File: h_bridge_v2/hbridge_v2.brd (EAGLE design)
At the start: 92.3 x 48.2 mm, 28 parts, among them J2 1X2-3.5MM, J3 1X2-3.5MM, J4 AVR_SPI_PROG_3X2OFFSET_PADS, Q5 200mA/40V, Q6 200mA/40V, Q7 200mA/40V, Q8 200mA/40V, U1 328P, Y1 16MHz

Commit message: replaced the resonator with through hole one
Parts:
- removed Y1: 16MHz, SparkFun-Clocks:RESONATOR-SMD-3.2X1.3
- added Y2: (no value), SparkFun-Clocks:RESONATOR-PTH-7.6X3.8
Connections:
- net GND: now also Y2.2; no longer Y1.2
- net N$4: now also Y2.3; no longer Y1.3
- net N$5: now also Y2.1; no longer Y1.1
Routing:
- net GND: track 8.20 -> 2.41 mm
- net N$15: track 20.8 -> 25.1 mm
- net 5V: track 30.8 -> 33.2 mm
- net N$4: track 3.75 -> 4.88 mm

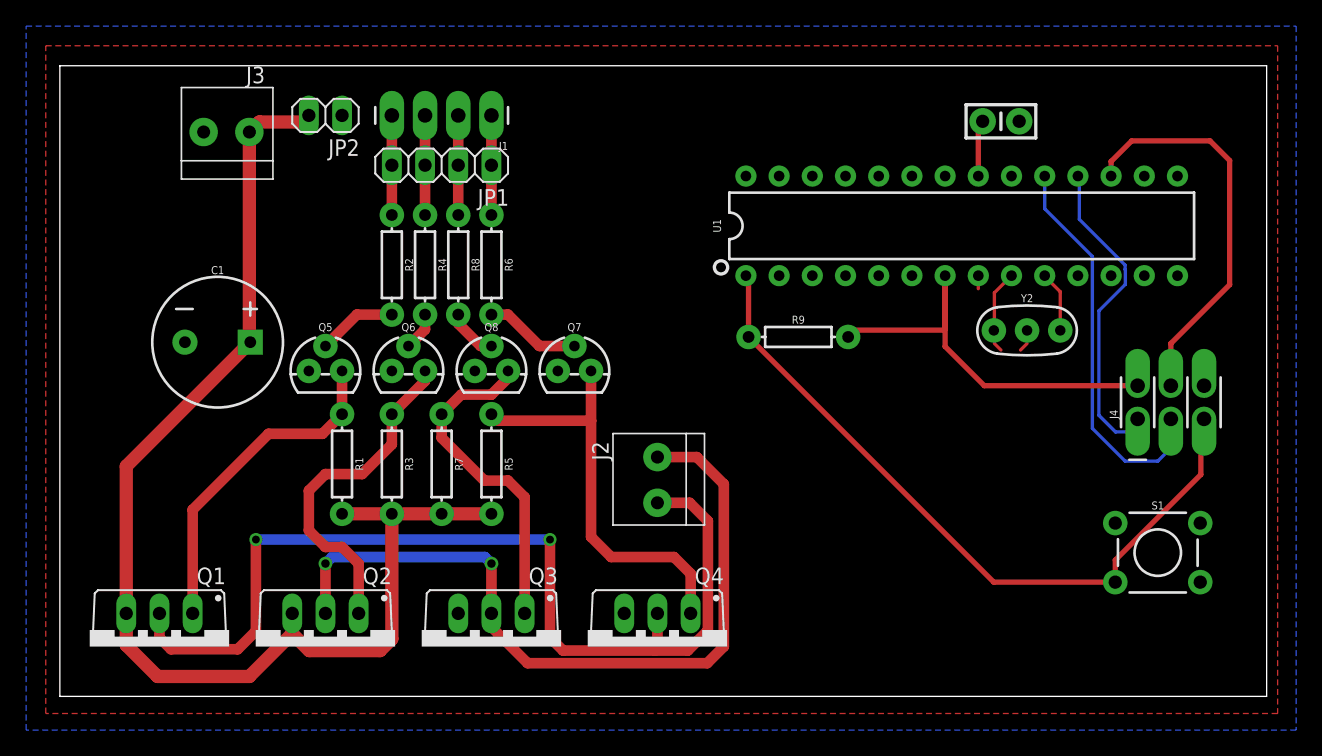
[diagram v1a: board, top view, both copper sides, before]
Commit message: added connections to PWM pins
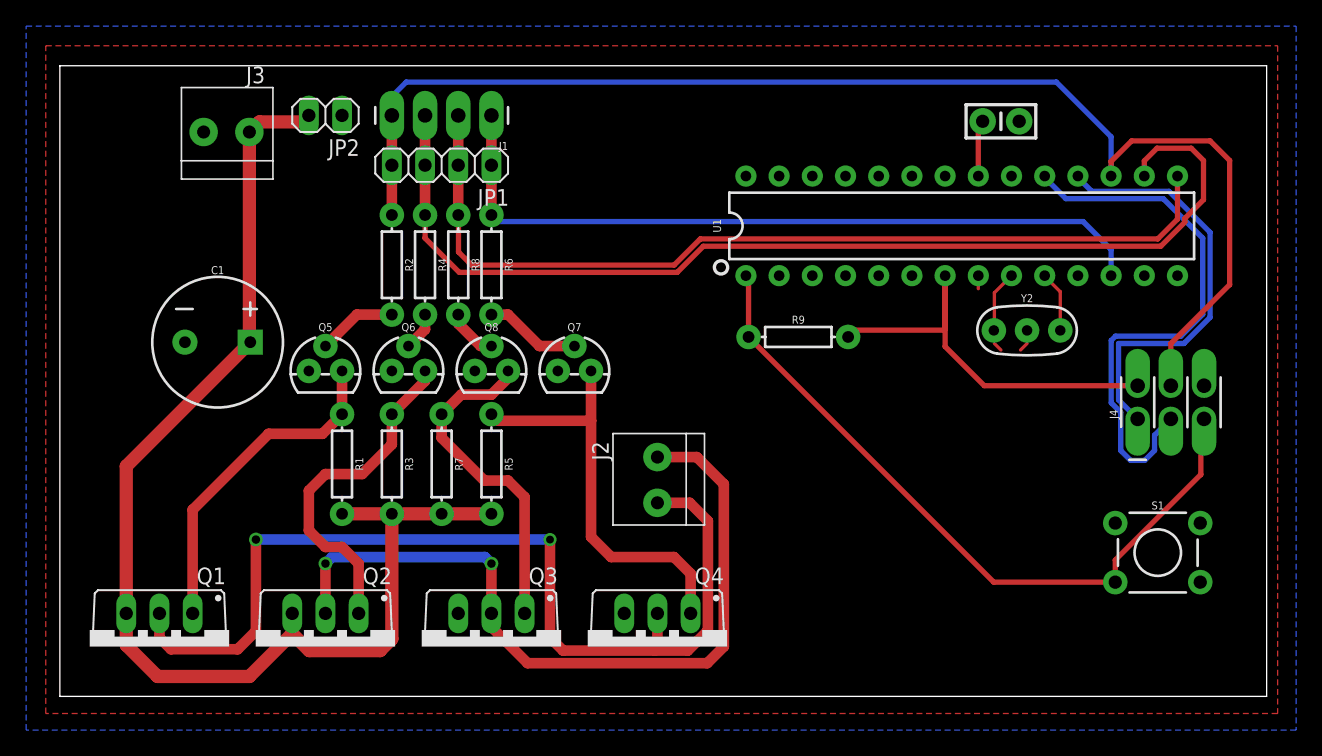
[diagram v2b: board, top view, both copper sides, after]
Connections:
- removed net N$18: J4.4, U1.17
- net Q1_INPUT: now also J4.4, U1.17
- net Q2_INPUT: now also U1.16
- net Q3_INPUT: now also U1.15
- net Q4_INPUT: now also U1.12
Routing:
- net Q1_INPUT: track 7.62 -> 99.8 mm
- net Q2_INPUT: track 7.62 -> 82.0 mm
- net Q3_INPUT: track 7.62 -> 70.6 mm
- net Q4_INPUT: track 7.62 -> 58.1 mm
- net N$18: track 30.6 -> 0.00 mm
- net N$16: track 30.5 -> 42.6 mm
- net N$15: track 25.1 -> 32.8 mm
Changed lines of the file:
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@@
 <drawing>
 <settings>
-<setting alwaysvectorfont="no"/>
+<setting alwaysvectorfont="yes"/>
 <setting verticaltext="up"/>
 </settings>
@@
 <wire x1="38.5" y1="3.5052" x2="37.5" y2="4.5052" width="0.8128" layer="1"/>
 <via x="37.5" y="12" extent="1-16" drill="0.6"/>
-<via x="15" y="12" extent="1-16" drill="0.6"/>
+<via x="15" y="12" extent="1-16" drill="0.65"/>
 <wire x1="15" y1="12" x2="15" y2="5" width="0.8128" layer="1"/>
 <wire x1="37.5" y1="4.5052" x2="37.5" y2="12" width="0.8128" layer="1"/>
@@
 <wire x1="27.94" y1="44.45" x2="27.94" y2="40.64" width="0.8128" layer="1"/>
 <wire x1="27.94" y1="36.83" x2="27.94" y2="40.64" width="0.8128" layer="1"/>
+<contactref element="U1" pad="16"/>
+<wire x1="82.97" y1="39.81" x2="82.97" y2="40.97" width="0.4064" layer="1"/>
+<wire x1="82.97" y1="40.97" x2="83.9412" y2="41.9412" width="0.4064" layer="1"/>
+<wire x1="86.5588" y1="41.9412" x2="87.5" y2="41" width="0.4064" layer="1"/>
+<wire x1="87.5" y1="41" x2="87.5" y2="38" width="0.4064" layer="1"/>
+<wire x1="86.0688" y1="36.5688" x2="86.0688" y2="36.27853125" width="0.4064" layer="1"/>
+<wire x1="86.0688" y1="36.27853125" x2="84.23146875" y2="34.4412" width="0.4064" layer="1"/>
+<wire x1="87.5" y1="38" x2="86.0688" y2="36.5688" width="0.4064" layer="1"/>
+<wire x1="49.23146875" y1="34.4412" x2="47.23146875" y2="32.4412" width="0.4064" layer="1"/>
+<wire x1="47.23146875" y1="32.4412" x2="30.5588" y2="32.4412" width="0.4064" layer="1"/>
+<wire x1="84.23146875" y1="34.4412" x2="49.23146875" y2="34.4412" width="0.4064" layer="1"/>
+<wire x1="27.94" y1="35.06" x2="27.94" y2="36.83" width="0.4064" layer="1"/>
+<wire x1="83.9412" y1="41.9412" x2="86.5588" y2="41.9412" width="0.4064" layer="1"/>
+<wire x1="30.5588" y1="32.4412" x2="27.94" y2="35.06" width="0.4064" layer="1"/>
 </signal>
 <signal name="N$6">
@@
 <wire x1="25.4" y1="44.45" x2="25.4" y2="40.64" width="0.8128" layer="1"/>
 <wire x1="25.4" y1="40.64" x2="25.4" y2="36.83" width="0.8128" layer="1"/>
+<contactref element="J4" pad="4"/>
+<contactref element="U1" pad="17"/>
+<wire x1="85" y1="23.77" x2="85" y2="27" width="0.4064" layer="1"/>
+<wire x1="89.5" y1="31.5" x2="89.5" y2="41" width="0.4064" layer="1"/>
+<wire x1="89.5" y1="41" x2="88" y2="42.5" width="0.4064" layer="1"/>
+<wire x1="88" y1="42.5" x2="82" y2="42.5" width="0.4064" layer="1"/>
+<wire x1="82" y1="42.5" x2="80.43" y2="40.93" width="0.4064" layer="1"/>
+<wire x1="80.43" y1="40.93" x2="80.43" y2="39.81" width="0.4064" layer="1"/>
+<wire x1="85" y1="27" x2="89.5" y2="31.5" width="0.4064" layer="1"/>
+<wire x1="25.4" y1="44.45" x2="25.4" y2="45.9" width="0.4064" layer="16"/>
+<wire x1="25.4" y1="45.9" x2="26.5" y2="47" width="0.4064" layer="16"/>
+<wire x1="26.5" y1="47" x2="76.24" y2="47" width="0.4064" layer="16"/>
+<wire x1="80.43" y1="42.81" x2="80.43" y2="39.81" width="0.4064" layer="16"/>
+<wire x1="80.43" y1="42.81" x2="76.24" y2="47" width="0.4064" layer="16"/>
 </signal>
 <signal name="Q4_INPUT">
@@
 <wire x1="33.02" y1="36.83" x2="33.02" y2="40.64" width="0.8128" layer="1"/>
 <wire x1="33.02" y1="40.64" x2="33.02" y2="44.45" width="0.8128" layer="1"/>
+<contactref element="U1" pad="12"/>
+<wire x1="78.29" y1="36.33" x2="33.52" y2="36.33" width="0.4064" layer="16"/>
+<wire x1="33.02" y1="36.83" x2="33.52" y2="36.33" width="0.4064" layer="16"/>
+<wire x1="80.43" y1="34.19" x2="80.43" y2="32.19" width="0.4064" layer="16"/>
+<wire x1="80.43" y1="34.19" x2="78.29" y2="36.33" width="0.4064" layer="16"/>
 </signal>
 <signal name="Q3_INPUT">
@@
 <wire x1="30.48" y1="36.83" x2="30.48" y2="40.64" width="0.8128" layer="1"/>
 <wire x1="30.48" y1="40.64" x2="30.48" y2="44.45" width="0.8128" layer="1"/>
+<contactref element="U1" pad="15"/>
+<wire x1="85.51" y1="39.81" x2="85.51" y2="36.51" width="0.4064" layer="1"/>
+<wire x1="85.51" y1="36.51" x2="84" y2="35" width="0.4064" layer="1"/>
+<wire x1="84" y1="35" x2="49" y2="35" width="0.4064" layer="1"/>
+<wire x1="47" y1="33" x2="31.5" y2="33" width="0.4064" layer="1"/>
+<wire x1="31.5" y1="33" x2="30.5" y2="34" width="0.4064" layer="1"/>
+<wire x1="30.5" y1="34" x2="30.5" y2="36.81" width="0.4064" layer="1"/>
+<wire x1="30.5" y1="36.81" x2="30.48" y2="36.83" width="0.4064" layer="1"/>
+<wire x1="49" y1="35" x2="47" y2="33" width="0.4064" layer="1"/>
 </signal>
 <signal name="N$4">
@@
 <contactref element="J4" pad="1"/>
 <wire x1="77.89" y1="39.81" x2="78" y2="39.7" width="0.254" layer="16"/>
-<wire x1="78" y1="39.7" x2="78" y2="36.5" width="0.254" layer="16"/>
-<wire x1="78" y1="36.5" x2="81.5" y2="33" width="0.254" layer="16"/>
-<wire x1="81.5" y1="32.66460625" x2="81.5222" y2="32.64240625" width="0.254" layer="16"/>
-<wire x1="81.5222" y1="32.64240625" x2="81.5222" y2="31.5222" width="0.254" layer="16"/>
-<wire x1="81.5" y1="33" x2="81.5" y2="32.66460625" width="0.254" layer="16"/>
-<wire x1="81.5222" y1="31.5222" x2="79.5" y2="29.5" width="0.254" layer="16"/>
-<wire x1="79.5" y1="29.5" x2="79.5" y2="21.5" width="0.254" layer="16"/>
-<wire x1="79.5" y1="21.5" x2="80.77" y2="20.23" width="0.254" layer="16"/>
-<wire x1="82.46" y1="20.23" x2="82.46" y2="21.23" width="0.254" layer="16"/>
-<wire x1="82.46" y1="20.23" x2="80.77" y2="20.23" width="0.254" layer="16"/>
+<wire x1="84.8584" y1="38.6416" x2="88" y2="35.5" width="0.4064" layer="16"/>
+<wire x1="78.94603125" y1="38.6416" x2="77.89" y2="39.69763125" width="0.4064" layer="16"/>
+<wire x1="77.89" y1="39.81" x2="77.89" y2="39.69763125" width="0.4064" layer="16"/>
+<wire x1="78.94603125" y1="38.6416" x2="84.8584" y2="38.6416" width="0.4064" layer="16"/>
+<wire x1="88" y1="35.5" x2="88" y2="29" width="0.4064" layer="16"/>
+<wire x1="88" y1="29" x2="86" y2="27" width="0.4064" layer="16"/>
+<wire x1="86" y1="27" x2="81" y2="27" width="0.4064" layer="16"/>
+<wire x1="81" y1="27" x2="81" y2="22.69" width="0.4064" layer="16"/>
+<wire x1="81" y1="22.69" x2="82.46" y2="21.23" width="0.4064" layer="16"/>
 </signal>
 <signal name="N$16">
 <contactref element="U1" pad="19"/>
 <contactref element="J4" pad="3"/>
-<wire x1="79" y1="33.66" x2="75.35" y2="37.31" width="0.254" layer="16"/>
-<wire x1="75.35" y1="39.81" x2="75.35" y2="37.31" width="0.254" layer="16"/>
-<wire x1="79" y1="20.5" x2="81.5" y2="18" width="0.254" layer="16"/>
-<wire x1="81.5" y1="18" x2="84" y2="18" width="0.254" layer="16"/>
-<wire x1="84" y1="18" x2="85" y2="19" width="0.254" layer="16"/>
-<wire x1="85" y1="19" x2="85" y2="21.23" width="0.254" layer="16"/>
-<wire x1="79" y1="33.66" x2="79" y2="20.5" width="0.254" layer="16"/>
-</signal>
-<signal name="N$18">
-<contactref element="J4" pad="4"/>
-<contactref element="U1" pad="17"/>
-<wire x1="85" y1="23.77" x2="85" y2="27" width="0.4064" layer="1"/>
-<wire x1="89.5" y1="31.5" x2="89.5" y2="41" width="0.4064" layer="1"/>
-<wire x1="89.5" y1="41" x2="88" y2="42.5" width="0.4064" layer="1"/>
-<wire x1="88" y1="42.5" x2="82" y2="42.5" width="0.4064" layer="1"/>
-<wire x1="82" y1="42.5" x2="80.43" y2="40.93" width="0.4064" layer="1"/>
-<wire x1="80.43" y1="40.93" x2="80.43" y2="39.81" width="0.4064" layer="1"/>
-<wire x1="85" y1="27" x2="89.5" y2="31.5" width="0.4064" layer="1"/>
+<wire x1="83.7554" y1="18.813825" x2="82.996575" y2="18.055" width="0.4064" layer="16"/>
+<wire x1="82.996575" y1="18.055" x2="81.923425" y2="18.055" width="0.4064" layer="16"/>
+<wire x1="81.923425" y1="18.055" x2="81.1646" y2="18.813825" width="0.4064" layer="16"/>
+<wire x1="81.1646" y1="18.813825" x2="81.1646" y2="21.73513125" width="0.4064" layer="16"/>
+<wire x1="85" y1="21.23" x2="83.7554" y2="19.9854" width="0.4064" layer="16"/>
+<wire x1="83.7554" y1="19.9854" x2="83.7554" y2="18.813825" width="0.4064" layer="16"/>
+<wire x1="81.1646" y1="21.73513125" x2="80.4412" y2="22.45853125" width="0.4064" layer="16"/>
+<wire x1="80.4412" y1="27.23146875" x2="80.76853125" y2="27.5588" width="0.4064" layer="16"/>
+<wire x1="80.4412" y1="22.45853125" x2="80.4412" y2="27.23146875" width="0.4064" layer="16"/>
+<wire x1="80.76853125" y1="27.5588" x2="85.76853125" y2="27.5588" width="0.4064" layer="16"/>
+<wire x1="85.76853125" y1="27.5588" x2="87.4412" y2="29.23146875" width="0.4064" layer="16"/>
+<wire x1="84.4172" y1="38.0828" x2="76.96483125" y2="38.0828" width="0.4064" layer="16"/>
+<wire x1="76.96483125" y1="38.0828" x2="75.35" y2="39.69763125" width="0.4064" layer="16"/>
+<wire x1="75.35" y1="39.81" x2="75.35" y2="39.69763125" width="0.4064" layer="16"/>
+<wire x1="87.4412" y1="35.0588" x2="84.4172" y2="38.0828" width="0.4064" layer="16"/>
+<wire x1="87.4412" y1="29.23146875" x2="87.4412" y2="35.0588" width="0.4064" layer="16"/>
 </signal>
 </signals>

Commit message: added I2C port and some topnames
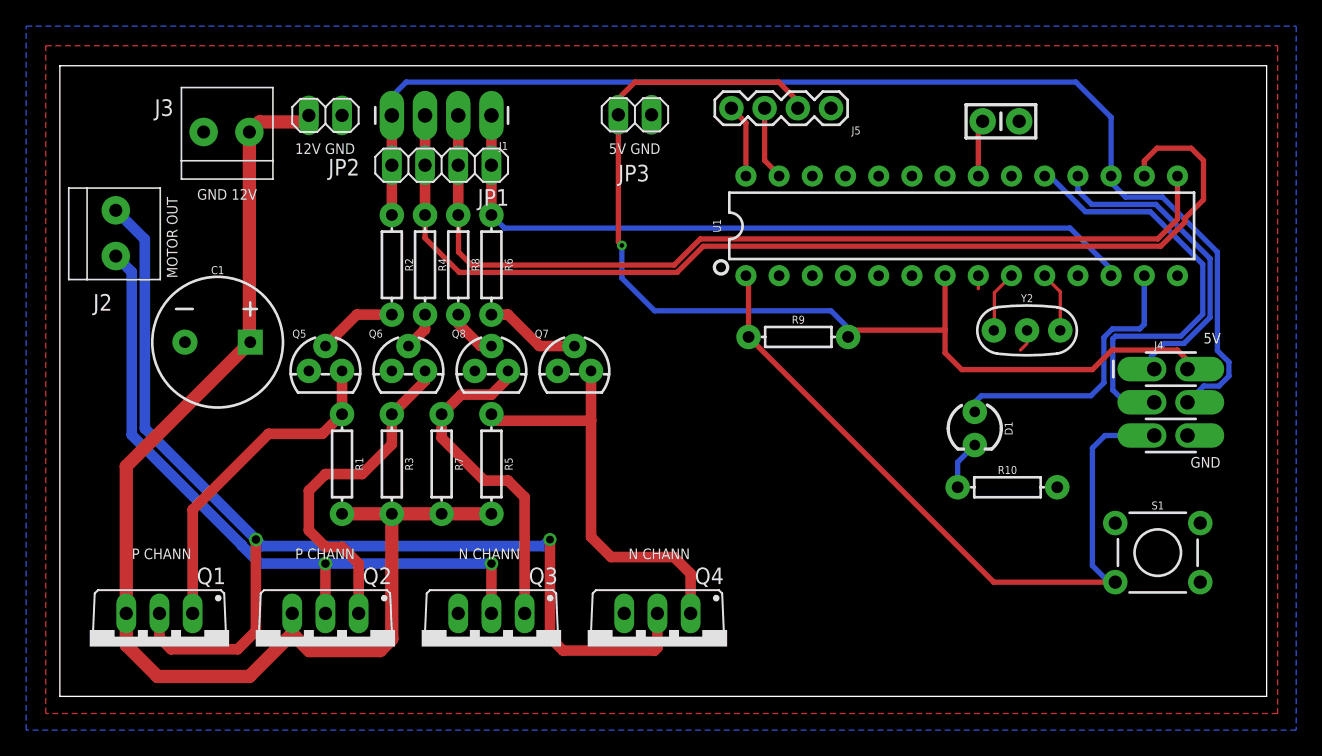
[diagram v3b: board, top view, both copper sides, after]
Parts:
- added D1: (no value), SparkFun-LED:LED_3MM
- added J5: (no value), SparkFun-Connectors:1X04
- added JP3: (no value), DC_LOAD_AU:1X02
- added R10: 1k, SparkFun-Resistors:AXIAL-0.3
- moved J2 45.6 mm to (4.28, 35.5), turned to 270 degrees
- turned J4 to 270 degrees
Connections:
- new net N$17: D1.A, U1.13
- new net N$18: D1.K, R10.P$1
- new net N$19: J5.3, U1.27
- new net N$20: J5.4, U1.28
- net 5V: now also J5.2, JP3.2
- net GND: now also J5.1, JP3.1, R10.P$2
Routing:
- net 5V: track 33.2 -> 83.1 mm, vias 0 -> 1
- net N$17: track 0.00 -> 21.9 mm
- net N$2: track 76.1 -> 88.6 mm
- net N$16: track 42.6 -> 33.8 mm
- net N$15: track 32.8 -> 24.8 mm
- net N$20: track 0.00 -> 5.65 mm
- net N$19: track 0.00 -> 5.65 mm
- net N$1: track 59.6 -> 54.5 mm
- net Q1_INPUT: track 99.8 -> 94.9 mm
- net N$18: track 0.00 -> 3.77 mm
- net N$7: track 55.9 -> 57.0 mm
- net Q4_INPUT: track 58.1 -> 57.2 mm
- net GND: track 2.41 -> 1.71 mm
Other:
- board text added: "12V GND"
- board text added: "5V"
- board text added: "5V GND"
- board text added: "GND"
- board text added: "GND 12V"
- board text added: "MOTOR OUT"
- board text added: "N CHANN"
- board text added: "P CHANN"
